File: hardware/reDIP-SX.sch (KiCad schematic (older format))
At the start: 82 parts, among them J1 DX07S016JA1, J10 Conn_01x01, J11 Conn_01x01, J2 Conn_01x01, J3 Conn_01x01, J4 Conn_01x01, J5 Conn_01x06, J6 Conn_01x06, J7 Conn_01x10, J8 Conn_01x10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

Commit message: Various fixes
* Added 10k pullup for SPI SCLK, following iCE40 Hardware Checklist
* Increased through hole pad sizes for USB-C connector
* Increased courtyard for TVSOP-56 footprint
* Changed VCC to power symbol
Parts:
- added R10: 10k, Resistor_SMD:R_0201_0603Metric, symbol Device:R
- U4: Notes (none) -> ALTERNATIVE PART #: SGTL5000XNLA3R2; PN SGTL5000XNLA3R2 -> SGTL5000XNLA3
- renumbered R10 to R11, R11 to R12, R12 to R13, U11 to U10, U10 to U11
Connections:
- net +3V3: now also R10.2
- net DTR: now also Q1.1 (E1), Q1.5 (B1); no longer Q1.2 (B1), Q1.4 (E1)
- net ESP_EN: now also Q1.3 (C1); no longer Q1.6 (C1)
- net RTS: now also Q1.2 (B1), Q1.4 (E1); no longer Q1.1 (E1), Q1.5 (B1)
- net SPI_SCLK: now also R10.1
- net SYS_CLK: now also Q1.6 (C1); no longer Q1.3 (C1)
- net Vcc renamed VCC
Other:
- moved on the sheet: J10, J11, J2, J3, J4, J5, J6, J7, J8, J9, U10, U11

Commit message: Replaced non-stocked parts
* Replaced 2 bit bus switch and 1.2V LDO with more readily available parts
* Length matching for SPI_SIO3 (note that length matching is probably uncalled-for)
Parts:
- U1: value NCP163AMX120TBG -> NCP115AMX120TCG; footprint ONSemi:CASE711AJ_1.0x1.0mm_P0.65mm -> ONSemi:CASE_711AJ_1.0x1.0mm_P0.65mm; symbol ONSemi:NCP163AMX120TBG -> ONSemi:NCP115AMX120TCG; Description IC REG LDO 1.2V 250mA XDFN4 -> IC REG LDO 1.2V 300mA XDFN4; PN NCP163AMX120TBG -> NCP115AMX120TCG
- U11: value CBTD3306GT -> 7WBD3306USG; footprint Nexperia:SOT-833-1 -> ONSemi:CASE_493-8_2.3x2mm_P0.5mm; symbol Nexperia:CBTD3306 -> ONSemi:7WBD3306USG; Description IC BUS SWITCH WITH LEVEL SHIFTER SOT833-1 -> IC BUS SWITCH WITH LEVEL SHIFTER US8; Mfg Nexperia -> ON Semiconductor; PN CBTD3306GT\\,115 -> 7WBD3306USG
- U2: footprint ONSemi:CASE711AJ_1.0x1.0mm_P0.65mm -> ONSemi:CASE_711AJ_1.0x1.0mm_P0.65mm
- U3: footprint ONSemi:523BC_1.4x1.8_P0.4mm -> ONSemi:CASE_523BC_1.4x1.8_P0.4mm
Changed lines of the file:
@@
 Sheet 1 1
 Title "reDIP SX"
-Date "2021-03-03"
+Date "2021-04-18"
 Rev "0.1"
 Comp "Nimrod"
@@
 F 0 "U2" H 5650 1715 50  0000 C CNN
 F 1 "NCP167AMX330TBG" H 5650 1624 50  0000 C CNN
-F 2 "ONSemi:CASE711AJ_1.0x1.0mm_P0.65mm" H 5650 1350 50  0001 C CNN
+F 2 "ONSemi:CASE_711AJ_1.0x1.0mm_P0.65mm" H 5650 1350 50  0001 C CNN
 F 3 "https://www.onsemi.com/pub/Collateral/NCP167-D.PDF" H 5650 1350 50  0001 C CNN
 F 4 "ON Semiconductor" H 5650 1350 50  0001 C CNN "Mfg"
@@
 $EndComp
 $Comp
-L ONSemi:NCP163AMX120TBG U1
+L ONSemi:NCP115AMX120TCG U1
 U 1 1 610BA994
 P 4000 1350
 F 0 "U1" H 4000 1715 50  0000 C CNN
-F 1 "NCP163AMX120TBG" H 4000 1624 50  0000 C CNN
-F 2 "ONSemi:CASE711AJ_1.0x1.0mm_P0.65mm" H 4000 1350 50  0001 C CNN
-F 3 "https://www.onsemi.com/pub/Collateral/NCP163-D.PDF" H 4000 1350 50  0001 C CNN
+F 1 "NCP115AMX120TCG" H 4000 1624 50  0000 C CNN
+F 2 "ONSemi:CASE_711AJ_1.0x1.0mm_P0.65mm" H 4000 1350 50  0001 C CNN
+F 3 "https://www.onsemi.com/pdf/datasheet/ncp115-d.pdf" H 4000 1350 50  0001 C CNN
 F 4 "ON Semiconductor" H 4000 1350 50  0001 C CNN "Mfg"
-F 5 "NCP163AMX120TBG" H 4000 1350 50  0001 C CNN "PN"
-F 6 "IC REG LDO 1.2V 250mA XDFN4" H 4000 1350 50  0001 C CNN "Description"
+F 5 "NCP115AMX120TCG" H 4000 1350 50  0001 C CNN "PN"
+F 6 "IC REG LDO 1.2V 300mA XDFN4" H 4000 1350 50  0001 C CNN "Description"
 	1    4000 1350
 	1    0    0    -1
@@
 F 0 "U3" H 3900 3000 50  0000 C CNN
 F 1 "FSA221UMX" H 4100 2900 50  0000 C CNN
-F 2 "ONSemi:523BC_1.4x1.8_P0.4mm" H 4100 3550 50  0001 C CNN
+F 2 "ONSemi:CASE_523BC_1.4x1.8_P0.4mm" H 4100 3550 50  0001 C CNN
 F 3 "https://www.onsemi.com/pub/Collateral/FSA221-D.pdf" H 4100 3550 50  0001 C CNN
 F 4 "ON Semiconductor" H 4100 3550 50  0001 C CNN "Mfg"
@@
 POT_Y
 $Comp
-L Nexperia:CBTD3306 U11
+L ONSemi:7WBD3306USG U11
 U 1 1 5F92F21C
 P 5750 8850
 F 0 "U11" H 5950 8450 50  0000 C CNN
-F 1 "CBTD3306GT" H 5750 8350 50  0000 C CNN
-F 2 "Nexperia:SOT-833-1" H 5750 8850 50  0001 C CNN
-F 3 "https://assets.nexperia.com/documents/data-sheet/CBTD3306.pdf" H 5750 8850 50  0001 C CNN
-F 4 "IC BUS SWITCH WITH LEVEL SHIFTER SOT833-1" H 5750 8850 50  0001 C CNN "Description"
-F 5 "Nexperia" H 5750 8850 50  0001 C CNN "Mfg"
-F 6 "CBTD3306GT\\,115" H 5750 8850 50  0001 C CNN "PN"
+F 1 "7WBD3306USG" H 5750 8350 50  0000 C CNN
+F 2 "ONSemi:CASE_493-8_2.3x2mm_P0.5mm" H 5750 8850 50  0001 C CNN
+F 3 "https://www.onsemi.com/pdf/datasheet/7wbd3306-d.pdf" H 5750 8850 50  0001 C CNN
+F 4 "IC BUS SWITCH WITH LEVEL SHIFTER US8" H 5750 8850 50  0001 C CNN "Description"
+F 5 "ON Semiconductor" H 5750 8850 50  0001 C CNN "Mfg"
+F 6 "7WBD3306USG" H 5750 8850 50  0001 C CNN "PN"
 	1    5750 8850
 	1    0    0    -1

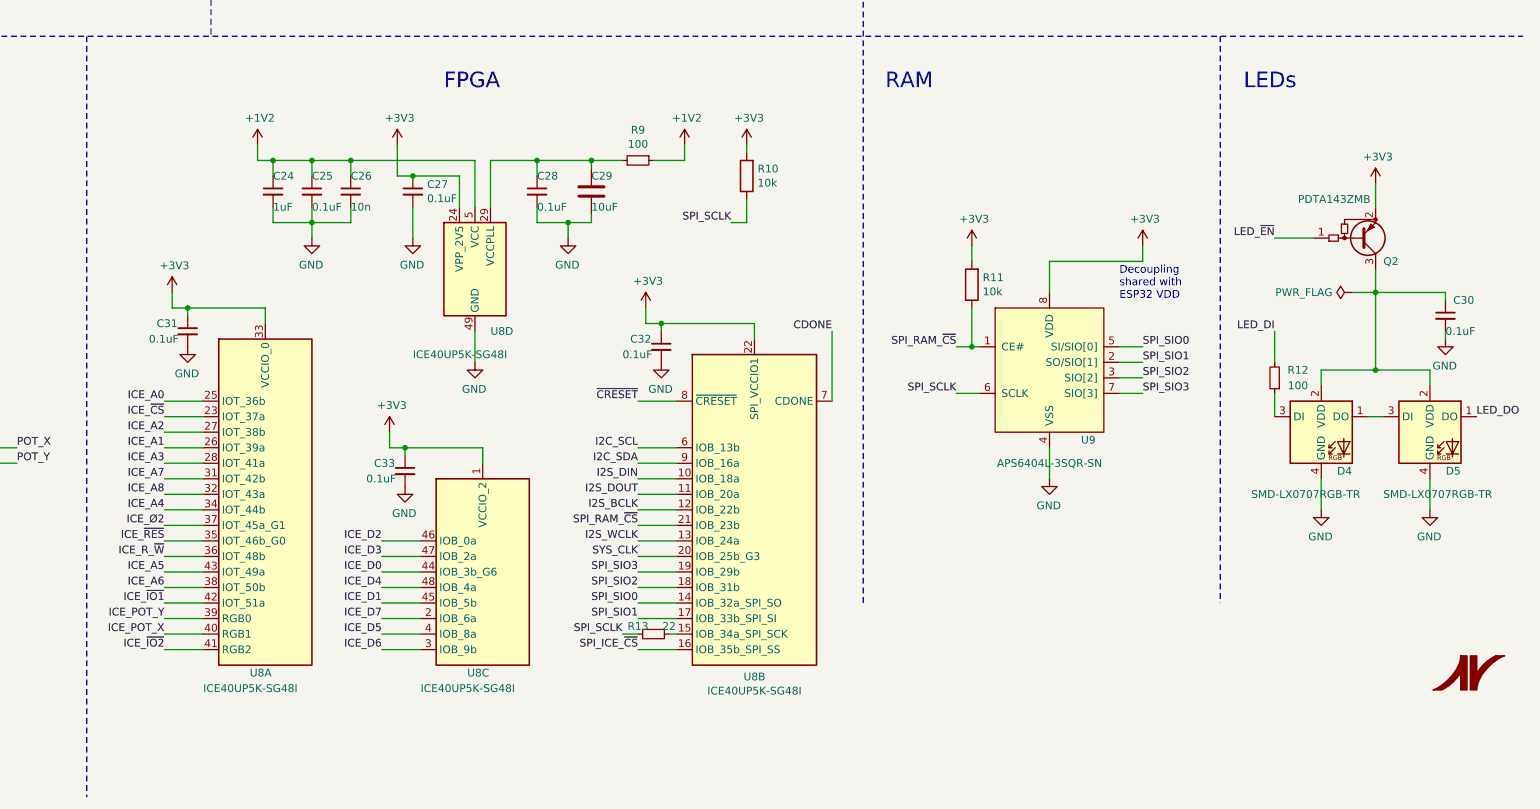
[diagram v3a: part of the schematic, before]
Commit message: Various improvements
* Improved decoupling and PLL power filtering,
  following suggestions by @smunaut for reDIP-SID
* Capped component position resolution to 0.01mm
* Routing cleanups
* Note on the iCE40 PLL output-only-pin trap in the schematic
* Added note on pin-in-paste for USB-C connector
* Moved KiCost BOM spreadsheet to documentation/
* Files for fabrication and assembly generated by KiKit
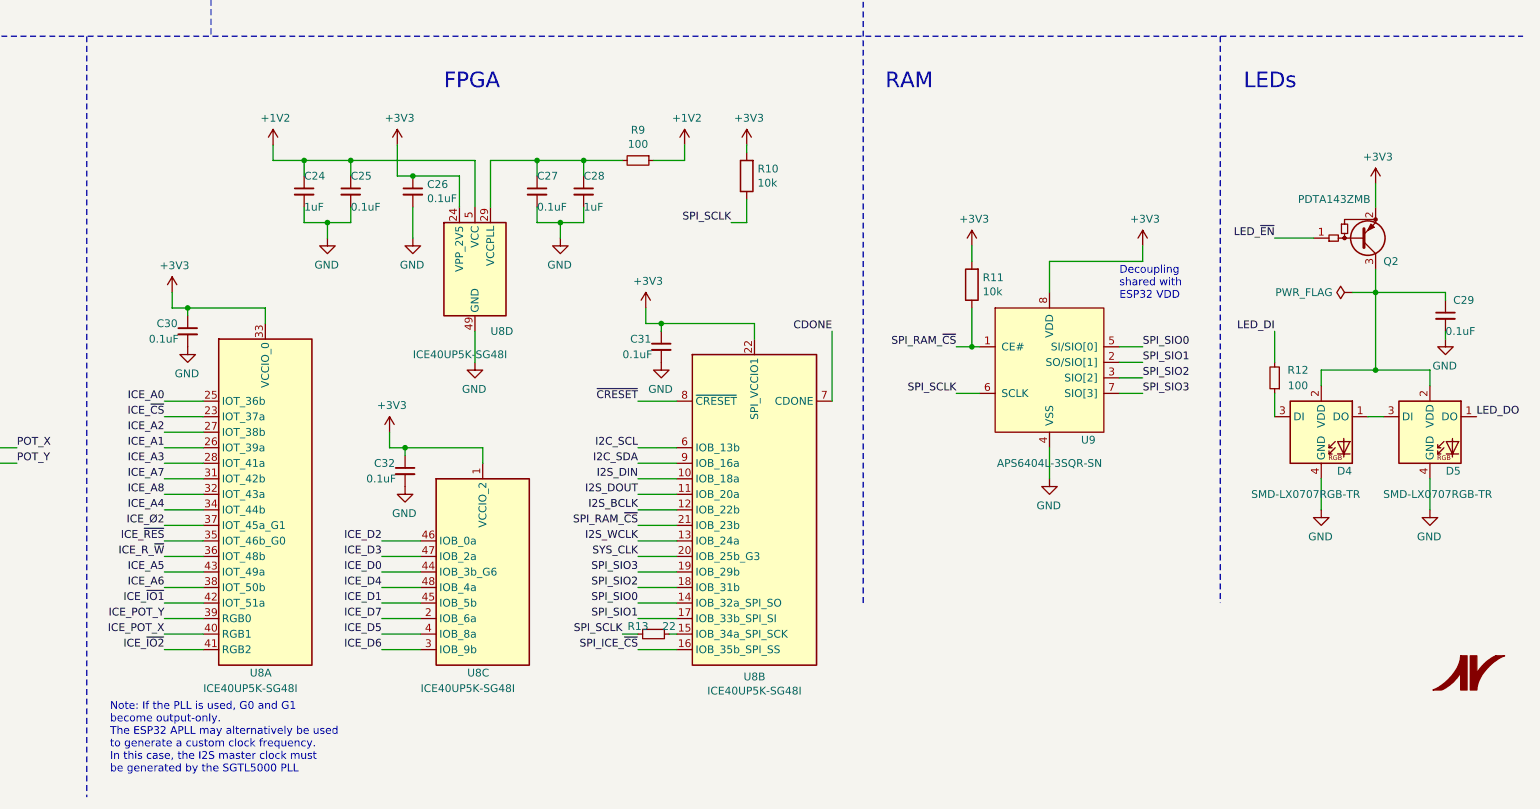
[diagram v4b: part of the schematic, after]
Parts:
- removed C26: 10n, Capacitor_SMD:C_0201_0603Metric, symbol Device:C_Small
- removed C29: 10uF, Capacitor_SMD:C_0402_1005Metric, symbol Device:C
- added C28: 1uF, Capacitor_SMD:C_0201_0603Metric, symbol Device:C_Small
- J1: Notes (none) -> PIN-IN-PASTE, paste overprinting included in design
- renumbered C27 to C26, C28 to C27, C30 to C29, C31 to C30, C32 to C31, C33 to C32
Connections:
- net GND: now also C28.2
- net at C27.1, R9.2, U8.29 (VCCPLL): now also C28.1
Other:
- note added: "Note: If the PLL is used, G0 and G1\nbecome output-only.\nThe ESP32 APLL may alternatively be used\nto generate a custom clock frequency.\nIn this case, the I2S master clock must\nbe generated by the SGTL5000 PLL"
- moved on the sheet: C24, C25
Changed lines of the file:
@@
 Sheet 1 1
 Title "reDIP SX"
-Date "2021-04-18"
-Rev "0.1"
+Date "2021-05-01"
+Rev "0.2"
 Comp "Nimrod"
 Comment1 "© 2020 - 2021 Dag Lem"
@@
 	10450 7100 10650 7100
 Wire Wire Line
-	10250 7100 10050 7100
-Wire Wire Line
 	9700 7100 9700 7200
 Connection ~ 9700 7100
@@
 	9700 7100 9400 7100
 Wire Wire Line
-	10050 7100 10050 7150
-Connection ~ 10050 7100
-Wire Wire Line
-	10050 7100 9700 7100
-Wire Wire Line
 	9700 7400 9700 7500
 Wire Wire Line
-	9700 7500 9900 7500
+	9700 7500 9850 7500
 $Comp
 L power:GND #PWR051
 U 1 1 5E6E1058
-P 9900 7600
-F 0 "#PWR051" H 9900 7350 50  0001 C CNN
-F 1 "GND" H 9905 7427 50  0000 C CNN
-F 2 "" H 9900 7600 50  0001 C CNN
-F 3 "" H 9900 7600 50  0001 C CNN
-	1    9900 7600
+P 9850 7600
+F 0 "#PWR051" H 9850 7350 50  0001 C CNN
+F 1 "GND" H 9855 7427 50  0000 C CNN
+F 2 "" H 9850 7600 50  0001 C CNN
+F 3 "" H 9850 7600 50  0001 C CNN
+	1    9850 7600
 	-1   0    0    -1
 $EndComp
-Wire Wire Line
-	10050 7450 10050 7500
 $Comp
 L power:GND #PWR062
@@
 	10500 8150 11100 8150
 Wire Wire Line
-	9900 7600 9900 7500
-Connection ~ 9900 7500
-Wire Wire Line
-	9900 7500 10050 7500
+	9850 7600 9850 7500
 $Comp
 L power:+1V2 #PWR043
 U 1 1 5EB96B60
-P 7900 7000
-F 0 "#PWR043" H 7900 6850 50  0001 C CNN
-F 1 "+1V2" H 7915 7173 50  0000 C CNN
-F 2 "" H 7900 7000 50  0001 C CNN
-F 3 "" H 7900 7000 50  0001 C CNN
-	1    7900 7000
+P 8000 7000
+F 0 "#PWR043" H 8000 6850 50  0001 C CNN
+F 1 "+1V2" H 8015 7173 50  0000 C CNN
+F 2 "" H 8000 7000 50  0001 C CNN
+F 3 "" H 8000 7000 50  0001 C CNN
+	1    8000 7000
 	1    0    0    -1
 $EndComp
 Wire Wire Line
-	8250 7500 8500 7500
-Connection ~ 8250 7500
-Wire Wire Line
-	8250 7400 8250 7500
-Wire Wire Line
-	8000 7500 8250 7500
+	8500 7400 8500 7500
 Wire Wire Line
-	8000 7400 8000 7500
+	8200 7500 8350 7500
 Wire Wire Line
-	8500 7500 8500 7400
-Wire Wire Line
-	8500 7100 8250 7100
-Connection ~ 8500 7100
+	8200 7400 8200 7500
 Wire Wire Line
 	8500 7100 8500 7200
 Wire Wire Line
-	8250 7100 8000 7100
-Connection ~ 8250 7100
-Wire Wire Line
-	8250 7100 8250 7200
-Wire Wire Line
-	8000 7100 7900 7100
-Connection ~ 8000 7100
-Wire Wire Line
-	8000 7100 8000 7200
-Wire Wire Line
-	7900 7100 7900 7000
+	8200 7100 8200 7200
 Wire Wire Line
-	9300 7100 8500 7100
+	8000 7100 8000 7000
 Wire Wire Line
-	8250 7600 8250 7500
+	8350 7600 8350 7500
 $Comp
 L power:GND #PWR049
 U 1 1 5E8FB01A
-P 8250 7600
-F 0 "#PWR049" H 8250 7350 50  0001 C CNN
-F 1 "GND" H 8255 7427 50  0000 C CNN
-F 2 "" H 8250 7600 50  0001 C CNN
-F 3 "" H 8250 7600 50  0001 C CNN
-	1    8250 7600
+P 8350 7600
+F 0 "#PWR049" H 8350 7350 50  0001 C CNN
+F 1 "GND" H 8355 7427 50  0000 C CNN
+F 2 "" H 8350 7600 50  0001 C CNN
+F 3 "" H 8350 7600 50  0001 C CNN
+	1    8350 7600
 	-1   0    0    -1
 $EndComp
@@
 $EndComp
 $Comp
-L Device:C C29
-U 1 1 5E5FEBE6
-P 10050 7300
-F 0 "C29" H 10050 7400 50  0000 L CNN
-F 1 "10uF" H 10050 7200 50  0000 L CNN
-F 2 "Capacitor_SMD:C_0402_1005Metric" H 10088 7150 50  0001 C CNN
-F 3 "https://www.murata.com/products/productdetail.aspx?partno=GRM155R60J106ME15D" H 10050 7300 50  0001 C CNN
-F 4 "Murata" H 10050 7300 50  0001 C CNN "Mfg"
-F 5 "GRM155R60J106ME15D" H 10050 7300 50  0001 C CNN "PN"
-F 6 "CAP CER 10uF 6.3V 20% X5R 0402" H 10050 7300 50  0001 C CNN "Description"
-F 7 "1.2V DC" H 10050 7300 50  0001 C CNN "Notes"
-	1    10050 7300
-	1    0    0    -1
-$EndComp
-$Comp
-L Device:C_Small C28
+L Device:C_Small C27
 U 1 1 5E5FFD7F
 P 9700 7300
-F 0 "C28" H 9700 7400 50  0000 L CNN
+F 0 "C27" H 9700 7400 50  0000 L CNN
 F 1 "0.1uF" H 9700 7200 50  0000 L CNN
 F 2 "Capacitor_SMD:C_0201_0603Metric" H 9700 7300 50  0001 C CNN
@@
 L Device:C_Small C24
 U 1 1 5E93F678
-P 8000 7300
-F 0 "C24" H 8000 7400 50  0000 L CNN
-F 1 "1uF" H 8000 7200 50  0000 L CNN
-F 2 "Capacitor_SMD:C_0201_0603Metric" H 8000 7300 50  0001 C CNN
-F 3 "https://www.murata.com/products/productdetail.aspx?partno=GRM033C80J105ME05D" H 8000 7300 50  0001 C CNN
-F 4 "Murata" H 8000 7300 50  0001 C CNN "Mfg"
-F 5 "GRM033C80J105ME05D" H 8000 7300 50  0001 C CNN "PN"
-F 6 "CAP CER 1uF 6.3V 20% X6S 0201" H 8000 7300 50  0001 C CNN "Description"
-F 7 "1.2V DC" H 8000 7300 50  0001 C CNN "Notes"
-	1    8000 7300
-	1    0    0    -1
-$EndComp
-$Comp
-L Device:C_Small C26
-U 1 1 5E8A1268
-P 8500 7300
-F 0 "C26" H 8500 7400 50  0000 L CNN
-F 1 "10n" H 8500 7200 50  0000 L CNN
-F 2 "Capacitor_SMD:C_0201_0603Metric" H 8500 7300 50  0001 C CNN
-F 3 "https://www.murata.com/products/productdetail.aspx?partno=GRM033R60J103KA01D" H 8500 7300 50  0001 C CNN
-F 4 "Murata" H 8500 7300 50  0001 C CNN "Mfg"
-F 5 "GRM033R60J103KA01D" H 8500 7300 50  0001 C CNN "PN"
-F 6 "CAP CER 10nF 6.3V 10% X5R 0201" H 8500 7300 50  0001 C CNN "Description"
-F 7 "1.2V DC" H 8500 7300 50  0001 C CNN "Notes"
-	1    8500 7300
+P 8200 7300
+F 0 "C24" H 8200 7400 50  0000 L CNN
+F 1 "1uF" H 8200 7200 50  0000 L CNN
+F 2 "Capacitor_SMD:C_0201_0603Metric" H 8200 7300 50  0001 C CNN
+F 3 "https://www.murata.com/products/productdetail.aspx?partno=GRM033C80J105ME05D" H 8200 7300 50  0001 C CNN
+F 4 "Murata" H 8200 7300 50  0001 C CNN "Mfg"
+F 5 "GRM033C80J105ME05D" H 8200 7300 50  0001 C CNN "PN"
+F 6 "CAP CER 1uF 6.3V 20% X6S 0201" H 8200 7300 50  0001 C CNN "Description"
+F 7 "1.2V DC" H 8200 7300 50  0001 C CNN "Notes"
+	1    8200 7300
 	1    0    0    -1
 $EndComp
@@
 $EndComp
 $Comp
-L Device:C_Small C32
+L Device:C_Small C31
 U 1 1 5F4EE5D0
 P 10500 8300
-F 0 "C32" H 10300 8350 50  0000 L CNN
+F 0 "C31" H 10300 8350 50  0000 L CNN
 F 1 "0.1uF" H 10250 8250 50  0000 L CNN
 F 2 "Capacitor_SMD:C_0201_0603Metric" H 10500 8300 50  0001 C CNN
@@
 L Device:C_Small C25
 U 1 1 5E8A17F7
-P 8250 7300
-F 0 "C25" H 8250 7400 50  0000 L CNN
-F 1 "0.1uF" H 8250 7200 50  0000 L CNN
-F 2 "Capacitor_SMD:C_0201_0603Metric" H 8250 7300 50  0001 C CNN
-F 3 "https://www.murata.com/products/productdetail.aspx?partno=GRM033R60J224KE15D" H 8250 7300 50  0001 C CNN
-F 4 "Murata" H 8250 7300 50  0001 C CNN "Mfg"
-F 5 "GRM033R60J224KE15D" H 8250 7300 50  0001 C CNN "PN"
-F 6 "CAP CER 0.22uF 6.3V 20% X5R 0201" H 8250 7300 50  0001 C CNN "Description"
-F 7 "3.3V DC DERATED TO 0.1uF" H 8250 7300 50  0001 C CNN "Notes"
-	1    8250 7300
+P 8500 7300
+F 0 "C25" H 8500 7400 50  0000 L CNN
+F 1 "0.1uF" H 8500 7200 50  0000 L CNN
+F 2 "Capacitor_SMD:C_0201_0603Metric" H 8500 7300 50  0001 C CNN
+F 3 "https://www.murata.com/products/productdetail.aspx?partno=GRM033R60J224KE15D" H 8500 7300 50  0001 C CNN
+F 4 "Murata" H 8500 7300 50  0001 C CNN "Mfg"
+F 5 "GRM033R60J224KE15D" H 8500 7300 50  0001 C CNN "PN"
+F 6 "CAP CER 0.22uF 6.3V 20% X5R 0201" H 8500 7300 50  0001 C CNN "Description"
+F 7 "3.3V DC DERATED TO 0.1uF" H 8500 7300 50  0001 C CNN "Notes"
+	1    8500 7300
 	1    0    0    -1
 $EndComp
 $Comp
-L Device:C_Small C31
+L Device:C_Small C30
 U 1 1 5F460CD8
 P 7450 8200
-F 0 "C31" H 7250 8250 50  0000 L CNN
+F 0 "C30" H 7250 8250 50  0000 L CNN
 F 1 "0.1uF" H 7200 8150 50  0000 L CNN
 F 2 "Capacitor_SMD:C_0201_0603Metric" H 7450 8200 50  0001 C CNN
@@
 $EndComp
 $Comp
-L Device:C_Small C33
+L Device:C_Small C32
 U 1 1 5F3F233D
 P 8850 9100
-F 0 "C33" H 8650 9150 50  0000 L CNN
+F 0 "C32" H 8650 9150 50  0000 L CNN
 F 1 "0.1uF" H 8600 9050 50  0000 L CNN
 F 2 "Capacitor_SMD:C_0201_0603Metric" H 8850 9100 50  0001 C CNN
@@
 $EndComp
 $Comp
-L Device:C_Small C27
+L Device:C_Small C26
 U 1 1 612545C7
 P 8900 7300
-F 0 "C27" H 8992 7346 50  0000 L CNN
+F 0 "C26" H 8992 7346 50  0000 L CNN
 F 1 "0.1uF" H 8992 7255 50  0000 L CNN
 F 2 "Capacitor_SMD:C_0201_0603Metric" H 8900 7300 50  0001 C CNN
@@
 $EndComp
 $Comp
-L Device:C_Small C30
+L Device:C_Small C29
 U 1 1 5EBF6C70
 P 15550 8100
-F 0 "C30" H 15600 8200 50  0000 L CNN
+F 0 "C29" H 15600 8200 50  0000 L CNN
 F 1 "0.1uF" H 15550 8000 50  0000 L CNN
 F 2 "Capacitor_SMD:C_0201_0603Metric" H 15550 8100 50  0001 C CNN
@@
 F 5 "DX07S016JA1R1500" H 1400 4550 50  0001 C CNN "PN"
 F 6 "CONN USB-C" H 1400 4550 50  0001 C CNN "Description"
+F 7 "PIN-IN-PASTE, paste overprinting included in design" H 1400 4550 50  0001 C CNN "Notes"
 	1    1400 4550
 	1    0    0    -1
@@
 	950  1650 1300 1650
 Connection ~ 1300 1650
+Connection ~ 8500 7100
+Wire Wire Line
+	8500 7100 9300 7100
+Wire Wire Line
+	8000 7100 8200 7100
+$Comp
+L Device:C_Small C28
+U 1 1 60CF952A
+P 10000 7300
+F 0 "C28" H 10000 7400 50  0000 L CNN
+F 1 "1uF" H 10000 7200 50  0000 L CNN
+F 2 "Capacitor_SMD:C_0201_0603Metric" H 10000 7300 50  0001 C CNN
+F 3 "https://www.murata.com/products/productdetail.aspx?partno=GRM033C80J105ME05D" H 10000 7300 50  0001 C CNN
+F 4 "Murata" H 10000 7300 50  0001 C CNN "Mfg"
+F 5 "GRM033C80J105ME05D" H 10000 7300 50  0001 C CNN "PN"
+F 6 "CAP CER 1uF 6.3V 20% X6S 0201" H 10000 7300 50  0001 C CNN "Description"
+F 7 "1.2V DC" H 10000 7300 50  0001 C CNN "Notes"
+	1    10000 7300
+	1    0    0    -1
+$EndComp
+Wire Wire Line
+	9700 7100 10000 7100
+Wire Wire Line
+	10000 7200 10000 7100
+Connection ~ 10000 7100
+Wire Wire Line
+	10000 7100 10250 7100
+Connection ~ 9850 7500
+Wire Wire Line
+	9850 7500 10000 7500
+Wire Wire Line
+	10000 7500 10000 7400
+Connection ~ 8200 7100
+Wire Wire Line
+	8200 7100 8500 7100
+Connection ~ 8350 7500
+Wire Wire Line
+	8350 7500 8500 7500
+Text Notes 6950 11050 0    50   ~ 0
+Note: If the PLL is used, G0 and G1\nbecome output-only.\nThe ESP32 APLL may alternatively be used\nto generate a custom clock frequency.\nIn this case, the I2S master clock must\nbe generated by the SGTL5000 PLL
 $EndSCHEMATC
